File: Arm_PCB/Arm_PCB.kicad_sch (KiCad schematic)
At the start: 24 parts

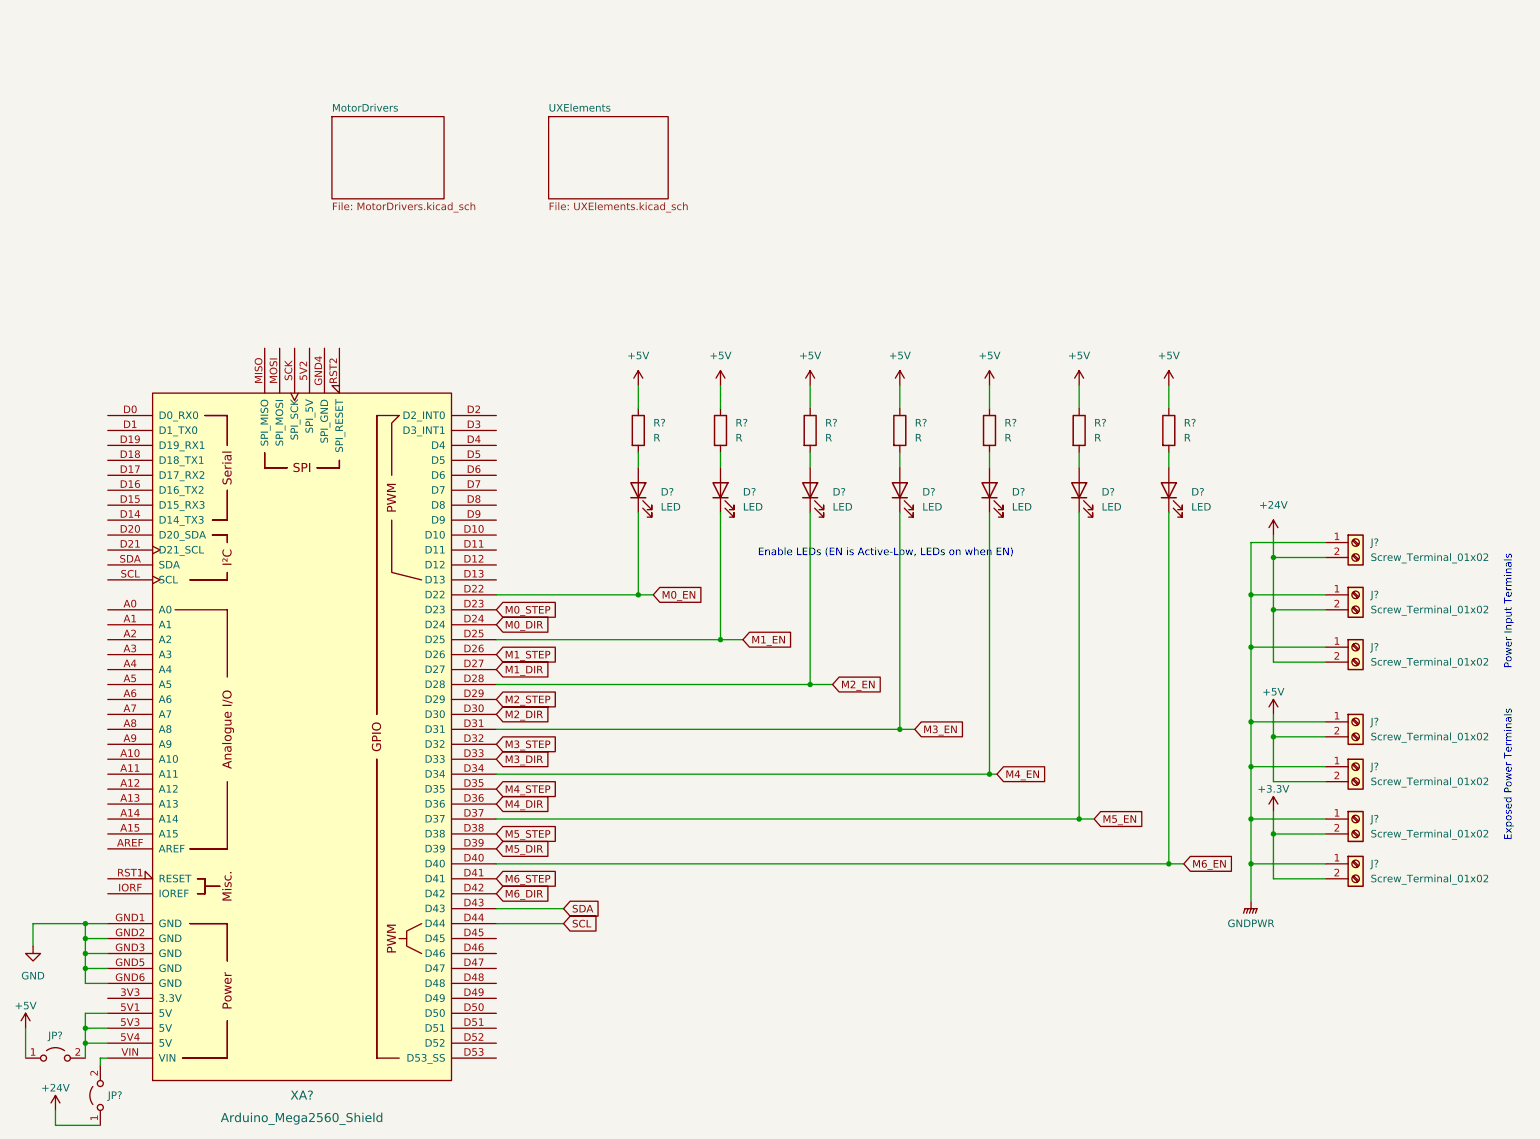
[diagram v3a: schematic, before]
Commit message: Changes, migrate to KiCad v7
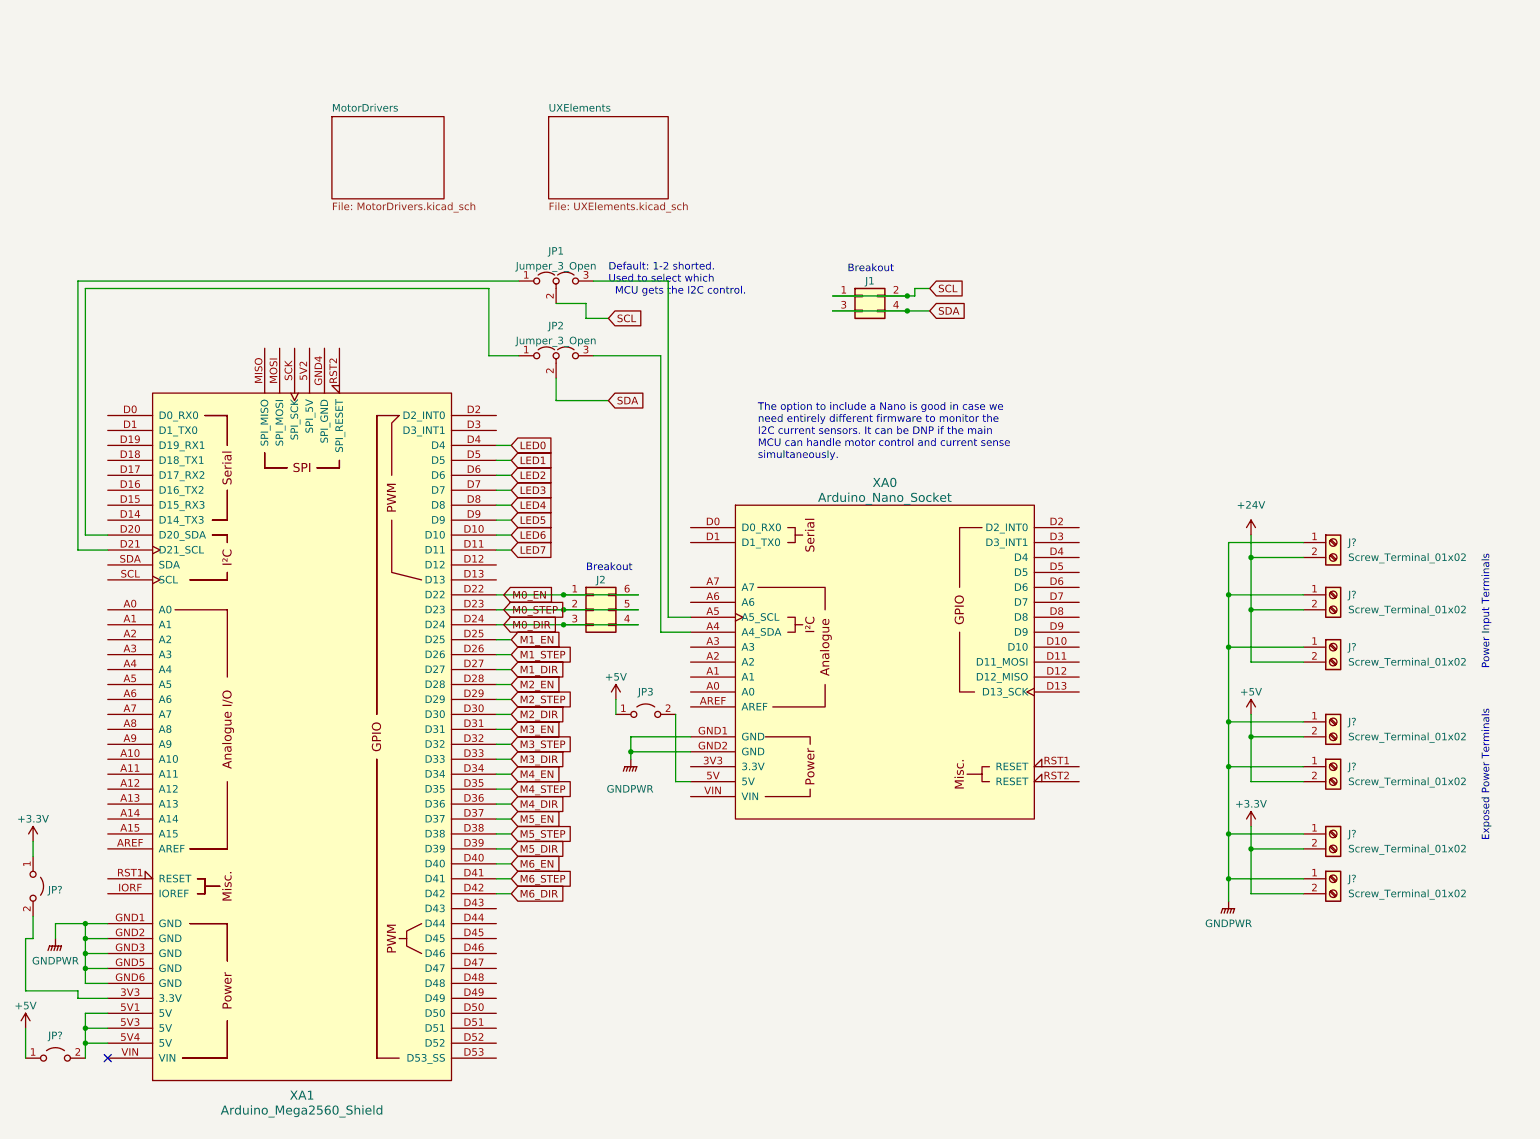
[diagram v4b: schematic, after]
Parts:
- removed D? (x7): LED, symbol Device:LED
- removed R? (x7): R, symbol Device:R
- added J1: Conn_02x02_Odd_Even, symbol Connector_Generic:Conn_02x02_Odd_Even
- added J2: Conn_02x03_Counter_Clockwise, symbol Connector_Generic:Conn_02x03_Counter_Clockwise
- added JP1, JP2: Jumper_3_Open, symbol Jumper:Jumper_3_Open
- added JP3: Jumper_2_Open, symbol Jumper:Jumper_2_Open
- added XA0: Arduino_Nano_Socket, Arduino_Library:Arduino_Nano_Socket, symbol Arduino_Library:Arduino_Nano_Socket
- gave numbers to parts that had none: 1
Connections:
- net GND is gone; now on net GNDPWR: XA1.GND1 (GND), XA1.GND2 (GND), XA1.GND3 (GND), XA1.GND5 (GND), XA1.GND6 (GND)
- net +24V: no longer JP?.1 (A)
- net +3.3V: now also JP?.1 (A)
- net +5V: now also JP3.1 (A)
- net GNDPWR: now also XA0.GND1 (GND), XA0.GND2 (GND)
- net M0_DIR: now also J2.3 (Pin_3), J2.4 (Pin_4)
- net M0_EN: now also J2.1 (Pin_1), J2.6 (Pin_6)
- net M0_STEP: now also J2.2 (Pin_2), J2.5 (Pin_5)
- net SCL: now also J1.1 (Pin_1), J1.2 (Pin_2), JP1.2 (C); no longer XA1.D44
- net SDA: now also J1.3 (Pin_3), J1.4 (Pin_4), JP2.2 (C); no longer XA1.D43
- net at XA1.3V3 (3.3V): now also JP?.2 (B)
- net LED6: now reaches XA1.D10
- net LED7: now reaches XA1.D11
- net at XA1.D20 (D20_SDA): now also JP2.1 (A)
- net at XA1.D21 (D21_SCL): now also JP1.1 (A)
- net LED0: now reaches XA1.D4
- net LED1: now reaches XA1.D5
- net LED2: now reaches XA1.D6
- net LED3: now reaches XA1.D7
- net LED4: now reaches XA1.D8
- net LED5: now reaches XA1.D9
- net at XA1.VIN: no longer JP?.2 (B)
- new net: JP3.2 (B), XA0.5V
- new net: JP2.3 (B), XA0.A4 (A4_SDA)
- new net: JP1.3 (B), XA0.A5 (A5_SCL)
- no-connect marks 0 -> 1
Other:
- note added: "Breakout"
- note added: "Default: 1-2 shorted. Used to select which MCU gets the I2C control."
- note added: "The option to include a Nano is good in case we need entirely different firmware to monitor the I2C current sensors. It can be DNP if the main MCU can handle motor control and current sense simultaneously."
- note removed: "Enable LEDs (EN is Active-Low, LEDs on when EN)"
- moved on the sheet: J?, JP?

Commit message: Changes, including UX and breakout pins
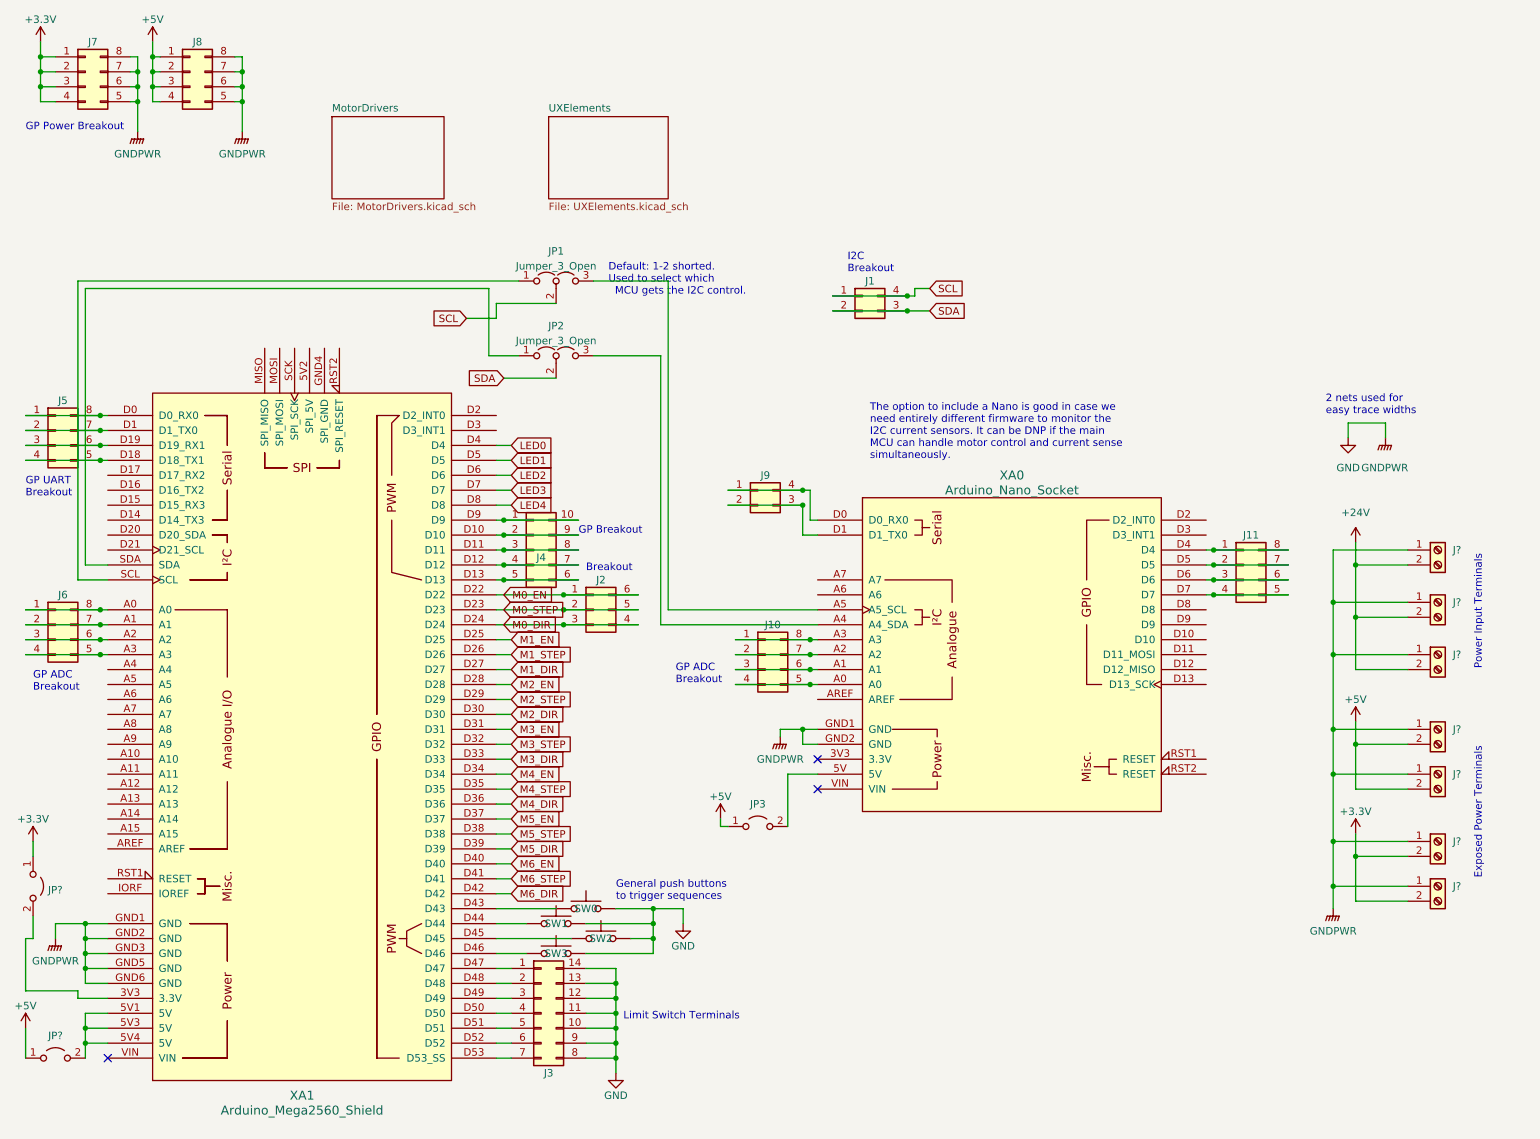
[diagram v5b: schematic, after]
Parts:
- removed J1: Conn_02x02_Odd_Even, symbol Connector_Generic:Conn_02x02_Odd_Even
- added J1, J9: Conn_02x02_Counter_Clockwise, symbol Connector_Generic:Conn_02x02_Counter_Clockwise
- added J10, J11, J5, J6, J7, J8: Conn_02x04_Counter_Clockwise, symbol Connector_Generic:Conn_02x04_Counter_Clockwise
- added J3: Conn_02x07_Counter_Clockwise, symbol Connector_Generic:Conn_02x07_Counter_Clockwise
- added J4: Conn_02x05_Counter_Clockwise, symbol Connector_Generic:Conn_02x05_Counter_Clockwise
- added SW0, SW1, SW2, SW3: SW_Push, symbol Switch:SW_Push
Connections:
- net +3.3V: now also J7.1 (Pin_1), J7.2 (Pin_2), J7.3 (Pin_3), J7.4 (Pin_4)
- net +5V: now also J8.1 (Pin_1), J8.2 (Pin_2), J8.3 (Pin_3), J8.4 (Pin_4)
- net SCL: now also J1.1 (Pin_1), J1.4 (Pin_4)
- net SDA: now also J1.2 (Pin_2), J1.3 (Pin_3)
- net at XA1.A0: now also J6.1 (Pin_1), J6.8 (Pin_8)
- net at XA1.A1: now also J6.2 (Pin_2), J6.7 (Pin_7)
- net at XA1.A2: now also J6.3 (Pin_3), J6.6 (Pin_6)
- net at XA1.A3: now also J6.4 (Pin_4), J6.5 (Pin_5)
- net at XA1.D0 (D0_RX0): now also J5.1 (Pin_1), J5.8 (Pin_8)
- net at XA1.D1 (D1_TX0): now also J5.2 (Pin_2), J5.7 (Pin_7)
- net at XA1.D12: now also J4.4 (Pin_4), J4.7 (Pin_7)
- net at XA1.D13: now also J4.5 (Pin_5), J4.6 (Pin_6)
- net at XA1.D18 (D18_TX1): now also J5.4 (Pin_4), J5.5 (Pin_5)
- net at XA1.D19 (D19_RX1): now also J5.3 (Pin_3), J5.6 (Pin_6)
- net at XA1.D20 (D20_SDA): no longer JP2.1 (A)
- net at XA1.D21 (D21_SCL): no longer JP1.1 (A)
- net at XA1.D43: now also SW0.1
- net at XA1.D44: now also SW1.1
- net at XA1.D45: now also SW2.1
- net at XA1.D46: now also SW3.1
- net at XA1.D47: now also J3.1 (Pin_1)
- net at XA1.D48: now also J3.2 (Pin_2)
- net at XA1.D49: now also J3.3 (Pin_3)
- net at XA1.D50: now also J3.4 (Pin_4)
- net at XA1.D51: now also J3.5 (Pin_5)
- net at XA1.D52: now also J3.6 (Pin_6)
- net at XA1.D53 (D53_SS): now also J3.7 (Pin_7)
- net at XA1.SCL: now also JP1.1 (A)
- net at XA1.SDA: now also JP2.1 (A)
- net at XA0.A0: now also J10.4 (Pin_4), J10.5 (Pin_5)
- net at XA0.A1: now also J10.3 (Pin_3), J10.6 (Pin_6)
- net at XA0.A2: now also J10.2 (Pin_2), J10.7 (Pin_7)
- net at XA0.A3: now also J10.1 (Pin_1), J10.8 (Pin_8)
- net at XA0.D0 (D0_RX0): now also J9.1 (Pin_1), J9.4 (Pin_4)
- net at XA0.D1 (D1_TX0): now also J9.2 (Pin_2), J9.3 (Pin_3)
- net at XA0.D4: now also J11.1 (Pin_1), J11.8 (Pin_8)
- net at XA0.D5: now also J11.2 (Pin_2), J11.7 (Pin_7)
- net at XA0.D6: now also J11.3 (Pin_3), J11.6 (Pin_6)
- net at XA0.D7: now also J11.4 (Pin_4), J11.5 (Pin_5)
- net GNDPWR renamed GND
- net GND: now also J3.10 (Pin_10), J3.11 (Pin_11), J3.12 (Pin_12), J3.13 (Pin_13), J3.14 (Pin_14), J3.8 (Pin_8), J3.9 (Pin_9), J7.5 (Pin_5), J7.6 (Pin_6), J7.7 (Pin_7), J7.8 (Pin_8), J8.5 (Pin_5), J8.6 (Pin_6), J8.7 (Pin_7), J8.8 (Pin_8), SW0.2, SW1.2, SW2.2, SW3.2
- net LED5: no longer names the net of XA1.D9
- net LED5: now also J4.1 (Pin_1), J4.10 (Pin_10)
- net LED6: no longer names the net of XA1.D10
- net LED6: now also J4.2 (Pin_2), J4.9 (Pin_9)
- net LED7: no longer names the net of XA1.D11
- net LED7: now also J4.3 (Pin_3), J4.8 (Pin_8)
- no-connect marks 1 -> 3
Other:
- note added: "2 nets used for easy trace widths"
- note added: "GP ADC Breakout"
- note added: "GP Breakout"
- note added: "GP Power Breakout"
- note added: "GP UART Breakout"
- note added: "General push buttons to trigger sequences"
- note added: "I2C Breakout"
- note added: "Limit Switch Terminals"
- moved on the sheet: J?, JP3, XA0
